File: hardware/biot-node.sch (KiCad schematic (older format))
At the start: 11 parts, among them J1 MPU9250 connection, J2 3.3V DC, P1 ATSAMR21B, P2 ATSAMR21B-TEST-POINTs, P3 ATMEL-CORTEX, P4 FTDI/Serial, SW1 Reset

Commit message: Adding latest biot node circuits.
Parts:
- removed J2: 3.3V DC, Pin_Headers:Pin_Header_Straight_1x02_Pitch2.54mm, symbol CONN_01X02
- removed P1: ATSAMR21B, Pin_Headers:Pin_Header_Straight_1x07_Pitch2.00mm, symbol CONN_01X07
- removed P2: ATSAMR21B-TEST-POINTs, Pin_Headers:Pin_Header_Straight_1x05_Pitch2.54mm, symbol CONN_01X05
- removed P3: ATMEL-CORTEX, atmelSAM:ATMEL_cortex_header_smd, symbol CONN_02X05
- removed SW1: Reset, Buttons_Switches_SMD:SW_SPST_EVPBF, symbol SW_PUSH_SMALL
- added 3.6VNiMH1: Battery, atsamr21:varta_3V80H_Battery, symbol Battery
- added C1: 1uF, Capacitors_SMD:C_1206, symbol C_Small
- added C2: 4.7uF, Capacitors_SMD:C_1206, symbol C_Small
- added J1: Test Points, Pin_Headers:Pin_Header_Straight_1x02_Pitch2.54mm_SMD_Pin1Right, symbol Conn_01x02
- added J4: ATMEL-CORTEX, Pin_Headers:Pin_Header_Straight_2x05_Pitch1.27mm_SMD, symbol Conn_02x05_Odd_Even
- added SW1: SW_Reset, Buttons_Switches_SMD:SW_SPST_B3S-1000, symbol SW_Push
- added U1: ATSAMR21B18-MZ210PA, atsamr21:ATSAMR21B18-MZ210PA, symbol ATSAMR21B18-MZ210PA
- added U2: LP2985-3.3, TO_SOT_Packages_SMD:SOT-23-5, symbol LP2985-3.3
- D1, D2: symbol Led_Small -> LED_Small
- J2: renamed from J1; symbol CONN_01X04 -> Conn_01x04
- P1: renamed from P4; footprint Pin_Headers:Pin_Header_Straight_1x06_Pitch2.54mm -> Pin_Headers:Pin_Header_Straight_1x06_Pitch2.54mm_SMD_Pin1Right; symbol CONN_01X06 -> Conn_01x06
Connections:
- net labels added: PA14, PA15
- wire segments 20 -> 23
- no-connect marks 7 -> 6
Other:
- note removed: "TP4"
- note removed: "TP5"
- moved on the sheet: D1, D2, R1, R2

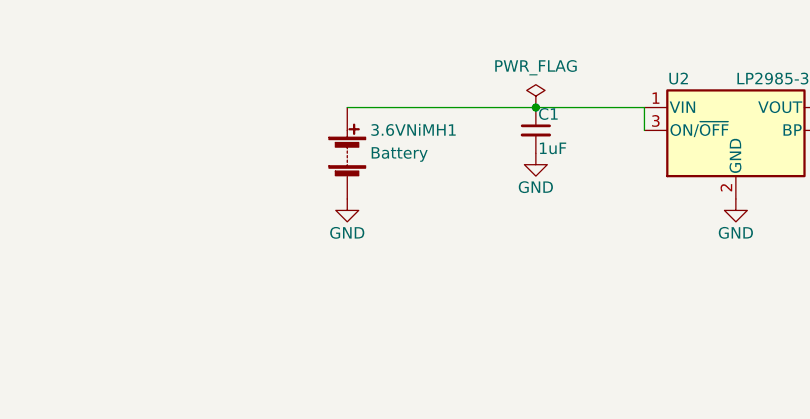
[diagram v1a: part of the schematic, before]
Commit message: Hardware with CR123 battery holder.
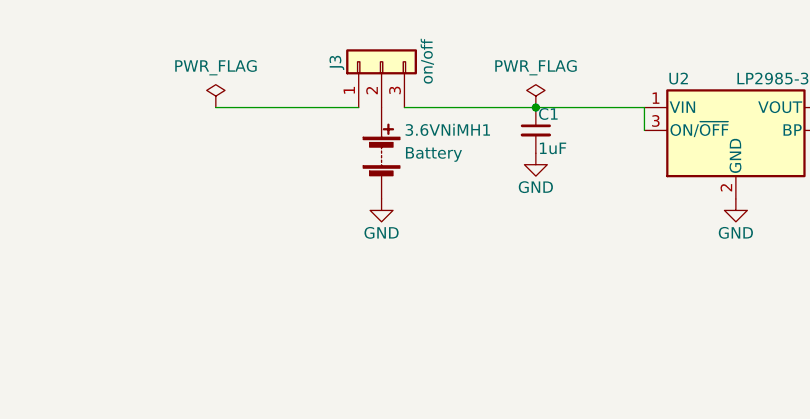
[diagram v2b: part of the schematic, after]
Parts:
- added J3: on/off, Pin_Headers:Pin_Header_Straight_1x03_Pitch2.54mm_SMD_Pin1Right, symbol Conn_01x03
- 3.6VNiMH1: footprint atsamr21:varta_3V80H_Battery -> atsamr21:CR123_Battery_Holder
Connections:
- net at C1.1, U2.1 (VIN), U2.3 (ON/~OFF~): now also J3.3 (Pin_3); no longer 3.6VNiMH1.1 (+)
- new net: 3.6VNiMH1.1 (+), J3.2 (Pin_2)
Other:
- moved on the sheet: 3.6VNiMH1
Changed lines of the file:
@@
 EESchema Schematic File Version 2
-LIBS:biot-node-rescue
 LIBS:power
 LIBS:device
@@
 	8700 1725 9850 1725
 Wire Wire Line
-	6600 1725 7900 1725
+	6850 1725 7900 1725
 Wire Wire Line
 	7900 1725 7900 1825
@@
 L GND #PWR016
 U 1 1 5A822113
-P 6600 2125
-F 0 "#PWR016" H 6600 1875 50  0001 C CNN
-F 1 "GND" H 6600 1975 50  0000 C CNN
-F 2 "" H 6600 2125 50  0000 C CNN
-F 3 "" H 6600 2125 50  0000 C CNN
-	1    6600 2125
+P 6750 2125
+F 0 "#PWR016" H 6750 1875 50  0001 C CNN
+F 1 "GND" H 6750 1975 50  0000 C CNN
+F 2 "" H 6750 2125 50  0000 C CNN
+F 3 "" H 6750 2125 50  0000 C CNN
+	1    6750 2125
 	1    0    0    -1
 $EndComp
@@
 L Battery 3.6VNiMH1
 U 1 1 5A8B66E0
-P 6600 1925
-F 0 "3.6VNiMH1" H 6700 2025 50  0000 L CNN
-F 1 "Battery" H 6700 1925 50  0000 L CNN
-F 2 "atsamr21:varta_3V80H_Battery" V 6600 1985 50  0001 C CNN
-F 3 "" V 6600 1985 50  0001 C CNN
-	1    6600 1925
-	1    0    0    -1
-$EndComp
+P 6750 1925
+F 0 "3.6VNiMH1" H 6850 2025 50  0000 L CNN
+F 1 "Battery" H 6850 1925 50  0000 L CNN
+F 2 "atsamr21:CR123_Battery_Holder" V 6750 1985 50  0001 C CNN
+F 3 "" V 6750 1985 50  0001 C CNN
+	1    6750 1925
+	1    0    0    -1
+$EndComp
+$Comp
+L Conn_01x03 J3
+U 1 1 5A94A810
+P 6750 1525
+F 0 "J3" H 6750 1725 50  0000 C CNN
+F 1 "on/off" H 6750 1325 50  0000 C CNN
+F 2 "Pin_Headers:Pin_Header_Straight_1x03_Pitch2.54mm_SMD_Pin1Right" H 6750 1525 50  0001 C CNN
+F 3 "" H 6750 1525 50  0001 C CNN
+	1    6750 1525
+	0    -1   -1   0
+$EndComp
+Wire Wire Line
+	6025 1725 6650 1725
+$Comp
+L PWR_FLAG #FLG018
+U 1 1 5A94C7FA
+P 6025 1725
+F 0 "#FLG018" H 6025 1820 50  0001 C CNN
+F 1 "PWR_FLAG" H 6025 1905 50  0000 C CNN
+F 2 "" H 6025 1725 50  0000 C CNN
+F 3 "" H 6025 1725 50  0000 C CNN
+	1    6025 1725
+	1    0    0    -1
+$EndComp

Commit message: Newer node hardware construction.
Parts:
- removed J1: Test Points, Pin_Headers:Pin_Header_Straight_1x02_Pitch2.54mm_SMD_Pin1Right, symbol Conn_01x02
- added J1: test points, Pin_Headers:Pin_Header_Straight_1x03_Pitch2.54mm_SMD_Pin1Right, symbol Conn_01x03
- 3.6VNiMH1: footprint atsamr21:CR123_Battery_Holder -> atsamr21:varta3v200h
- D1: value SIGNAL -> 20mA
- D2: value PWR -> 20mA
- R1, R2: value 39 -> 68
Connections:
- net GND: now also J1.2 (Pin_2)
- net PA14: now also J1.1 (Pin_1)
- net PA15: now also J1.3 (Pin_3)
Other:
- moved on the sheet: 3.6VNiMH1
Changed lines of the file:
@@
 P 9850 2125
 F 0 "D2" H 9800 2250 50  0000 L CNN
-F 1 "PWR" H 9675 2025 50  0000 L CNN
+F 1 "20mA" H 9775 2025 50  0000 L CNN
 F 2 "LEDs:LED_1206" V 9850 2125 50  0001 C CNN
 F 3 "" V 9850 2125 50  0000 C CNN
@@
 P 4825 4150
 F 0 "D1" H 4775 4275 50  0000 L CNN
-F 1 "SIGNAL" H 4650 4050 50  0000 L CNN
+F 1 "20mA" H 4725 4050 50  0000 L CNN
 F 2 "LEDs:LED_1206" V 4825 4150 50  0001 C CNN
 F 3 "" V 4825 4150 50  0000 C CNN
@@
 P 5075 4150
 F 0 "R1" V 5155 4150 50  0000 C CNN
-F 1 "39" V 5075 4150 50  0000 C CNN
+F 1 "68" V 5075 4150 50  0000 C CNN
 F 2 "Resistors_SMD:R_1210" V 5005 4150 50  0001 C CNN
 F 3 "" H 5075 4150 50  0000 C CNN
@@
 P 9850 1875
 F 0 "R2" V 9930 1875 50  0000 C CNN
-F 1 "39" V 9850 1875 50  0000 C CNN
+F 1 "68" V 9850 1875 50  0000 C CNN
 F 2 "Resistors_SMD:R_1210" V 9780 1875 50  0001 C CNN
 F 3 "" H 9850 1875 50  0000 C CNN
@@
 	1    0    0    -1
 $EndComp
-Wire Wire Line
-	5225 4150 5400 4150
-Wire Wire Line
-	3725 4150 4725 4150
-Wire Wire Line
-	3725 3650 5400 3650
-Wire Wire Line
-	8475 3800 8800 3800
 $Comp
 L GND #PWR04
@@
 	1    0    0    -1
 $EndComp
-Wire Wire Line
-	8425 4250 8825 4250
 $Comp
 L GND #PWR05
@@
 	1    0    0    -1
 $EndComp
-Wire Wire Line
-	7250 3425 7250 3575
 $Comp
 L +3.3V #PWR06
@@
 	1    0    0    -1
 $EndComp
-Wire Wire Line
-	4450 3550 3725 3550
-Wire Wire Line
-	4450 3050 4450 3550
 $Comp
 L +3.3V #PWR07
@@
 	1    0    0    -1
 $EndComp
-Wire Wire Line
-	8425 3400 8800 3400
 $Comp
 L +3.3V #PWR08
@@
 	1    0    0    -1
 $EndComp
-Wire Wire Line
-	8125 4275 8125 4450
-Wire Wire Line
-	8125 4450 8825 4450
-Wire Wire Line
-	8800 3600 8475 3600
-Wire Wire Line
-	8475 3500 8475 3800
-Wire Wire Line
-	8800 3500 8475 3500
-Connection ~ 8475 3600
-Wire Wire Line
-	5400 3650 5400 4150
 $Comp
 L PWR_FLAG #FLG09
@@
 	1    0    0    -1
 $EndComp
-Wire Wire Line
-	8275 5425 8775 5425
 Text GLabel 8775 5525 0    60   Input ~ 0
 SCLK
@@
 Text GLabel 2450 4525 3    60   Input ~ 0
 NRST
-$Comp
-L Conn_01x02 J1
-U 1 1 5A78D00A
-P 7325 5475
-F 0 "J1" H 7325 5575 50  0000 C CNN
-F 1 "Test Points" H 7325 5275 50  0000 C CNN
-F 2 "Pin_Headers:Pin_Header_Straight_1x02_Pitch2.54mm_SMD_Pin1Right" H 7325 5475 50  0001 C CNN
-F 3 "" H 7325 5475 50  0001 C CNN
-	1    7325 5475
-	1    0    0    -1
-$EndComp
-Text GLabel 7125 5475 0    60   Input ~ 0
+Text GLabel 7100 4725 0    60   Input ~ 0
 PA14
-Text GLabel 7125 5575 0    60   Input ~ 0
+Text GLabel 7100 4925 0    60   Input ~ 0
 PA15
 Text GLabel 2325 3250 1    60   Input ~ 0
@@
 L GND #PWR013
 U 1 1 5A821888
-P 8300 2125
-F 0 "#PWR013" H 8300 1875 50  0001 C CNN
-F 1 "GND" H 8300 1975 50  0000 C CNN
-F 2 "" H 8300 2125 50  0000 C CNN
-F 3 "" H 8300 2125 50  0000 C CNN
-	1    8300 2125
+P 8300 2450
+F 0 "#PWR013" H 8300 2200 50  0001 C CNN
+F 1 "GND" H 8300 2300 50  0000 C CNN
+F 2 "" H 8300 2450 50  0000 C CNN
+F 3 "" H 8300 2450 50  0000 C CNN
+	1    8300 2450
 	1    0    0    -1
 $EndComp
@@
 $EndComp
 NoConn ~ 8700 1825
-Wire Wire Line
-	8700 1725 9850 1725
-Wire Wire Line
-	6850 1725 7900 1725
-Wire Wire Line
-	7900 1725 7900 1825
-Connection ~ 7425 1725
 $Comp
 L GND #PWR016
 U 1 1 5A822113
-P 6750 2125
-F 0 "#PWR016" H 6750 1875 50  0001 C CNN
-F 1 "GND" H 6750 1975 50  0000 C CNN
-F 2 "" H 6750 2125 50  0000 C CNN
-F 3 "" H 6750 2125 50  0000 C CNN
-	1    6750 2125
-	1    0    0    -1
-$EndComp
-Wire Wire Line
-	9250 1725 9250 1525
+P 6750 2425
+F 0 "#PWR016" H 6750 2175 50  0001 C CNN
+F 1 "GND" H 6750 2275 50  0000 C CNN
+F 2 "" H 6750 2425 50  0000 C CNN
+F 3 "" H 6750 2425 50  0000 C CNN
+	1    6750 2425
+	1    0    0    -1
+$EndComp
 $Comp
 L +3.3V #PWR017
@@
 	1    0    0    -1
 $EndComp
-Connection ~ 9250 1725
-Wire Wire Line
-	9850 2225 9850 2350
-Connection ~ 9850 2275
-Wire Wire Line
-	9850 2275 9325 2275
-Wire Wire Line
-	9325 2275 9325 2300
 $Comp
 L Battery 3.6VNiMH1
 U 1 1 5A8B66E0
-P 6750 1925
-F 0 "3.6VNiMH1" H 6850 2025 50  0000 L CNN
-F 1 "Battery" H 6850 1925 50  0000 L CNN
-F 2 "atsamr21:CR123_Battery_Holder" V 6750 1985 50  0001 C CNN
-F 3 "" V 6750 1985 50  0001 C CNN
-	1    6750 1925
+P 6750 2225
+F 0 "3.6VNiMH1" H 6850 2325 50  0000 L CNN
+F 1 "Battery" H 6850 2225 50  0000 L CNN
+F 2 "atsamr21:varta3v200h" V 6750 2285 50  0001 C CNN
+F 3 "" V 6750 2285 50  0001 C CNN
+	1    6750 2225
 	1    0    0    -1
 $EndComp
@@
 	0    -1   -1   0
 $EndComp
-Wire Wire Line
-	6025 1725 6650 1725
 $Comp
 L PWR_FLAG #FLG018
@@
 	1    0    0    -1
 $EndComp
+$Comp
+L Conn_01x03 J1
+U 1 1 5AA9B3F4
+P 7300 4825
+F 0 "J1" H 7300 5025 50  0000 C CNN
+F 1 "test points" H 7300 4625 50  0000 C CNN
+F 2 "Pin_Headers:Pin_Header_Straight_1x03_Pitch2.54mm_SMD_Pin1Right" H 7300 4825 50  0001 C CNN
+F 3 "" H 7300 4825 50  0001 C CNN
+	1    7300 4825
+	1    0    0    -1
+$EndComp
+Wire Wire Line
+	5225 4150 5400 4150
+Wire Wire Line
+	3725 4150 4725 4150
+Wire Wire Line
+	3725 3650 5400 3650
+Wire Wire Line
+	8475 3800 8800 3800
+Wire Wire Line
+	8425 4250 8825 4250
+Wire Wire Line
+	7250 3425 7250 3575
+Wire Wire Line
+	4450 3550 3725 3550
+Wire Wire Line
+	4450 3050 4450 3550
+Wire Wire Line
+	8425 3400 8800 3400
+Wire Wire Line
+	8125 4275 8125 4450
+Wire Wire Line
+	8125 4450 8825 4450
+Wire Wire Line
+	8800 3600 8475 3600
+Wire Wire Line
+	8475 3500 8475 3800
+Wire Wire Line
+	8800 3500 8475 3500
+Connection ~ 8475 3600
+Wire Wire Line
+	5400 3650 5400 4150
+Wire Wire Line
+	8275 5425 8775 5425
+Wire Wire Line
+	8700 1725 9850 1725
+Wire Wire Line
+	6850 1725 7900 1725
+Wire Wire Line
+	7900 1725 7900 1825
+Connection ~ 7425 1725
+Wire Wire Line
+	9250 1725 9250 1525
+Connection ~ 9250 1725
+Wire Wire Line
+	9850 2225 9850 2350
+Connection ~ 9850 2275
+Wire Wire Line
+	9850 2275 9325 2275
+Wire Wire Line
+	9325 2275 9325 2300
+Wire Wire Line
+	6025 1725 6650 1725
+Wire Wire Line
+	6500 5125 6500 4825
+Wire Wire Line
+	6500 4825 7100 4825
+$Comp
+L GND #PWR019
+U 1 1 5AA9B987
+P 6500 5125
+F 0 "#PWR019" H 6500 4875 50  0001 C CNN
+F 1 "GND" H 6500 4975 50  0000 C CNN
+F 2 "" H 6500 5125 50  0000 C CNN
+F 3 "" H 6500 5125 50  0000 C CNN
+	1    6500 5125
+	1    0    0    -1
+$EndComp
+Wire Wire Line
+	6750 2025 6750 1725
+Connection ~ 7150 1725
+Wire Wire Line
+	8300 2125 8300 2450
+Connection ~ 8300 2250
 $EndSCHEMATC
